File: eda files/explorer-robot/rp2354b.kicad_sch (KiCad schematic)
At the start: 31 parts, among them J1 Conn_01x05, SW1 SW_Push, U1 RP2354B, U2 AMS1117-3.3, Y1 ABM8-272-T3

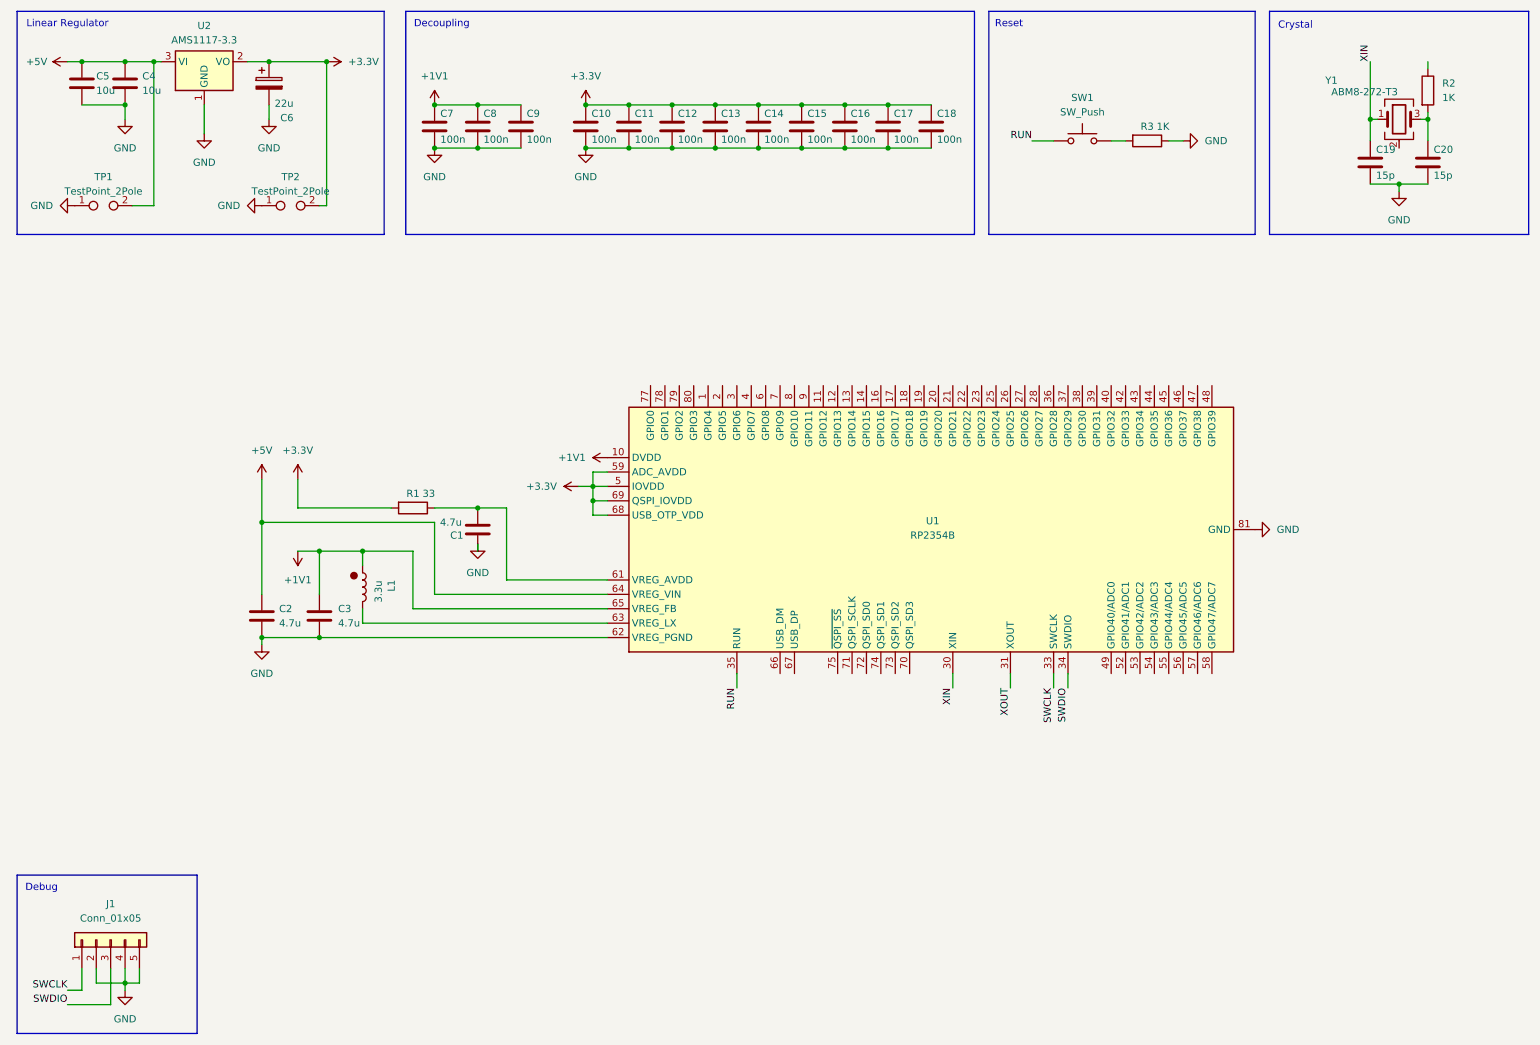
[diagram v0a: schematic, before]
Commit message: finish schematic for ICM-20948; requiring changes to pin assignment
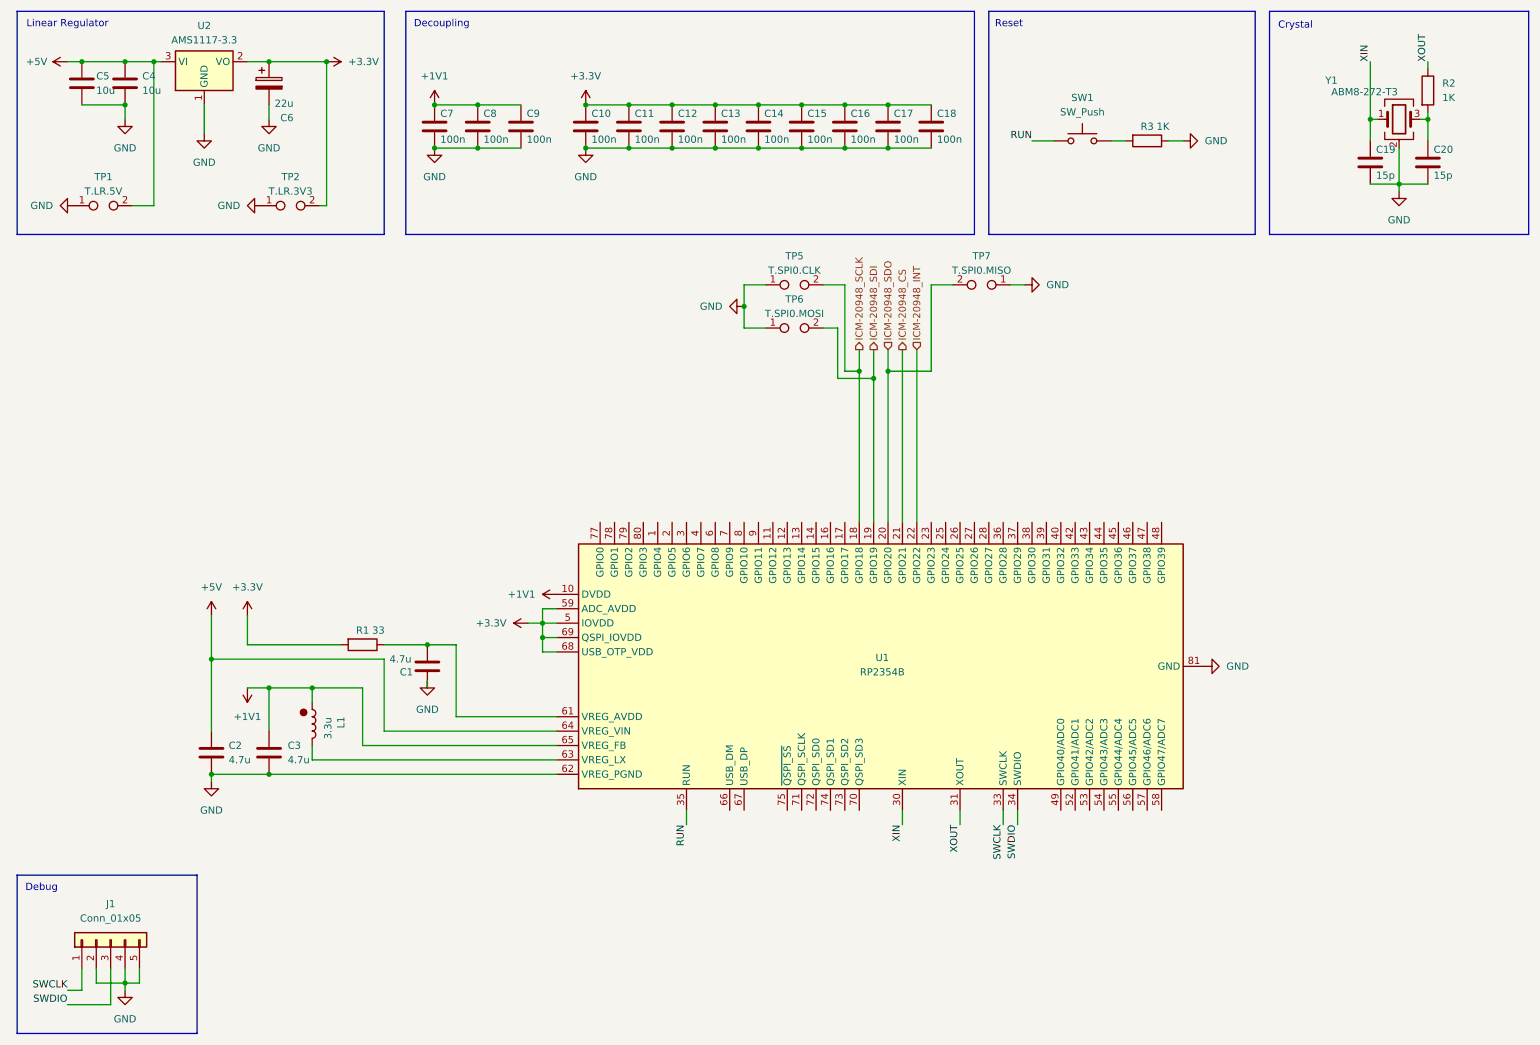
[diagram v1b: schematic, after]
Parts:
- added TP5: T.SPI0.CLK, tp:TestPoint_Bridge_Pitch3.81mm_Drill1.3mm, symbol Connector:TestPoint_2Pole
- added TP6: T.SPI0.MOSI, tp:TestPoint_Bridge_Pitch3.81mm_Drill1.3mm, symbol Connector:TestPoint_2Pole
- added TP7: T.SPI0.MISO, tp:TestPoint_Bridge_Pitch3.81mm_Drill1.3mm, symbol Connector:TestPoint_2Pole
- C1, C2, C3: LCSC https://jlcpcb.com/partdetail/24469-CL05A475MP5NRNC/C23733 -> C23733; MFR (none) -> Samsung Electro-Mechanics
- C10, C11, C12, C13, C14, C15, C16, C17, C18, C7, C8, C9: LCSC https://jlcpcb.com/partdetail/YAGEO-CC0603KRX7R9BB104/C14663 -> C14663; MFR (none) -> YAGEO; MPN C14663 -> CC0603KRX7R9BB104
- C19, C20: MFR (none) -> Samsung Electro-Mechanics
- C4, C5: LCSC https://jlcpcb.com/partdetail/20411-CL10A106KP8NNNC/C19702 -> C19702; MFR (none) -> Samsung Electro-Mechanics; MPN C19702 -> CL10A106KP8NNNC
- C6: LCSC https://jlcpcb.com/partdetail/-TAJA226K010RNJ/C11366 -> C11366; MFR (none) -> --; MPN C11366 -> TAJA226K010RNJ
- J1: LCSC https://jlcpcb.com/partdetail/Megastar-ZX_SH1_03PLT/C7430452 -> C7430452; MFR (none) -> Megastar; MPN C7430452 -> ZX-SH1.0-3PLT
- L1: LCSC https://jlcpcb.com/partdetail/AbraconLLC-AOTA_B201610S3R3_1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 -> C42411119; MFR (none) -> Abracon LLC; MPN C42411119 -> AOTA-B201610S3R3-101-T
- R1: LCSC https://jlcpcb.com/partdetail/25848-0402WGF330JTCE/C25105 -> 0402WGF330JTCE; MFR (none) -> UNI-ROYAL(Uniroyal Elec)
- R2: LCSC https://jlcpcb.com/partdetail/21904-0603WAF1001T5E/C21190 -> C21190; MFR (none) -> UNI-ROYAL(Uniroyal Elec); MPN C21190 -> 0603WAF1001T5E
- R3: LCSC https://jlcpcb.com/partdetail/12256-0402WGF1001TCE/C11702 -> C11702; MFR (none) -> UNI-ROYAL(Uniroyal Elec); MPN C11702 -> 0402WGF1001TCE
- SW1: LCSC https://jlcpcb.com/partdetail/XUNPU-TS_1088AR02016/C720477 -> C720477; MFR (none) -> XUNPU; MPN C720477 -> TS-1088-AR02016
- TP1: value TestPoint_2Pole -> T.LR.5V; footprint TestPoint:TestPoint_2Pads_Pitch5.08mm_Drill1.3mm -> tp:TestPoint_Bridge_Pitch3.81mm_Drill1.3mm
- TP2: value TestPoint_2Pole -> T.LR.3V3; footprint TestPoint:TestPoint_2Pads_Pitch5.08mm_Drill1.3mm -> tp:TestPoint_Bridge_Pitch3.81mm_Drill1.3mm
- U1: MFR (none) -> Raspberry Pi; MPN C39843328 -> RP2354B
- U2: LCSC https://jlcpcb.com/partdetail/Advanced_MonolithicSystems-AM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 -> C6186; MFR (none) -> Advanced Monolithic Systems; MPN C6186 -> AMS1117-3.3
- Y1: LCSC https://jlcpcb.com/partdetail/AbraconLLC-ABM8_272T3/C206257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 -> C20625731; MFR (none) -> Abracon LLC; MPN C20625731 -> ABM8-272-T3
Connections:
- net GND: now also Y1.2 (G), Y1.4 (G), TP5.1, TP6.1, TP7.1
- net XOUT: now also R2.1
- net ICM-20948_SCLK: now reaches U1.18 (GPIO18)
- net ICM-20948_SCLK: now also TP5.2
- net ICM-20948_SDI: now reaches U1.19 (GPIO19)
- net ICM-20948_SDI: now also TP6.2
- net ICM-20948_SDO: now reaches U1.20 (GPIO20)
- net ICM-20948_SDO: now also TP7.2
- net ICM-20948_CS: now reaches U1.21 (GPIO21)
- net ICM-20948_INT: now reaches U1.22 (GPIO22)
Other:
- title: (none) -> rp2354b and supporting components
- moved on the sheet: C1, C2, C3, L1, R1, U1

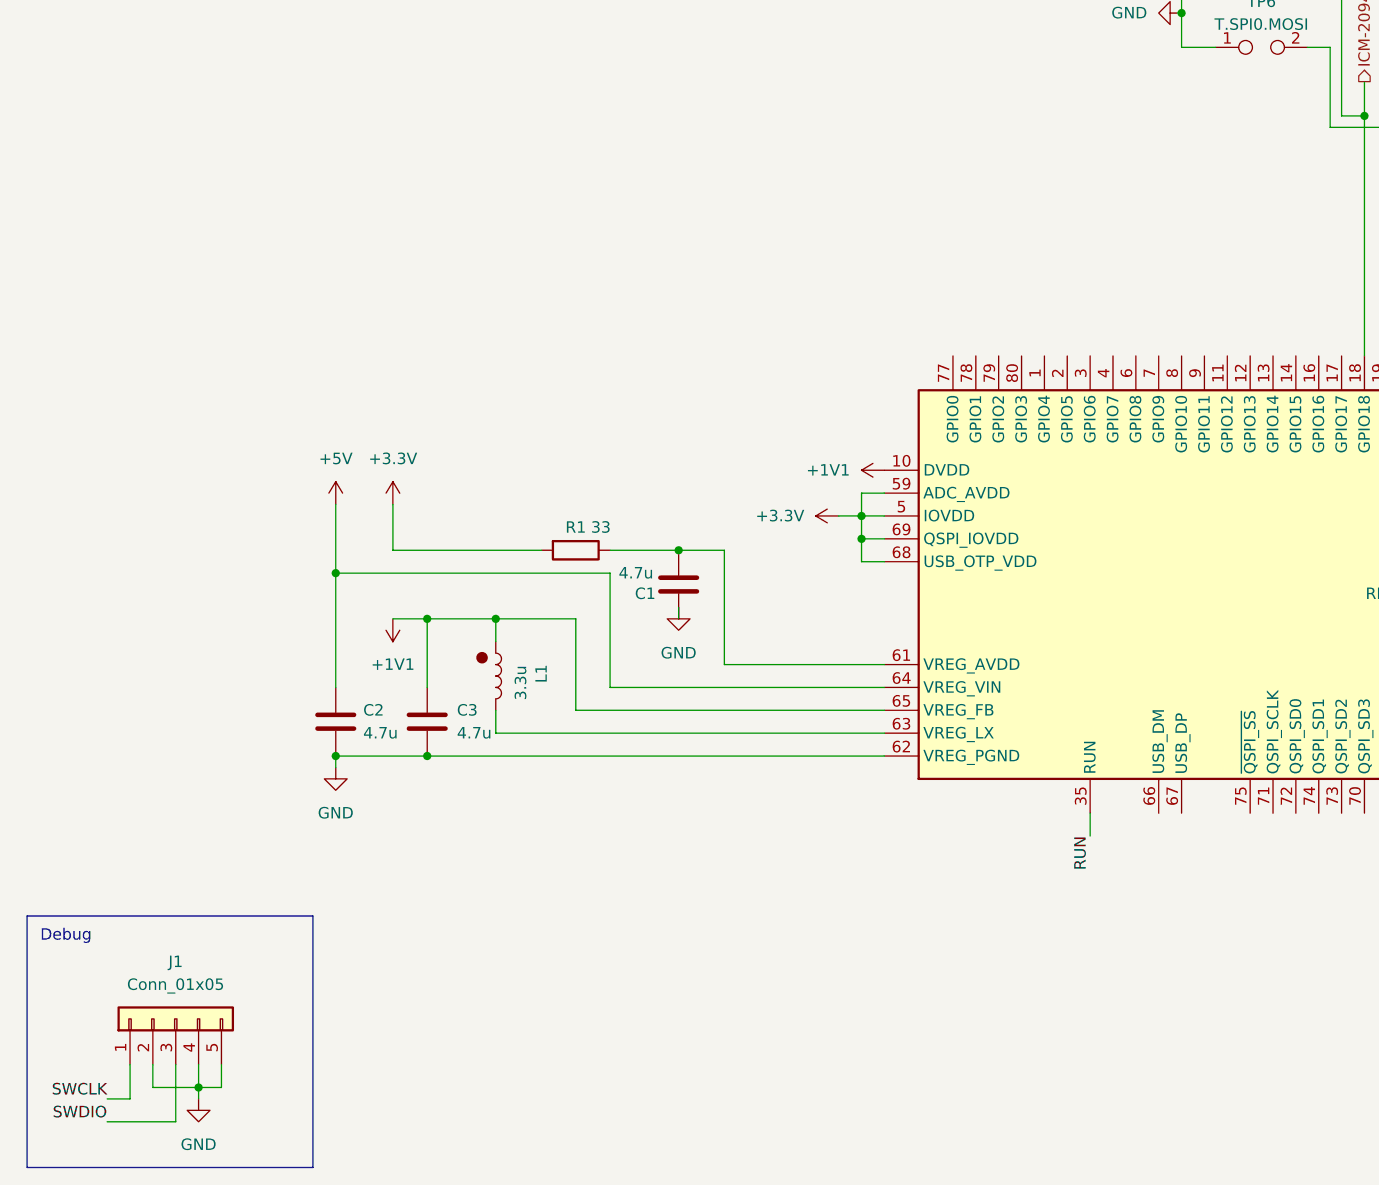
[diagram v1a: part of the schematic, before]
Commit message: Split power and motor driver into dedicated schematic sheets
Add ADRs 0018–0020 covering ground topology, battery rail and
connector protection decisions. Move battery, 5 V buck and test points
to a new power_and_batt sheet, and the TB6612FNG with motor connectors
to a new tb6612fng sheet.

Collapse the single ground net at the TB6612FNG, add the three-tier VM
decoupling stack and bidirectional TVS clamps on the motor pairs and VM.
Switch the 5 V rail to a TPS5430DDAR with a 220 µF/25 V polymer bulk
shared across the battery, VM and 5 V rails. Fix the ICM-20948 regulator
symbol to AMS1117-1.8.
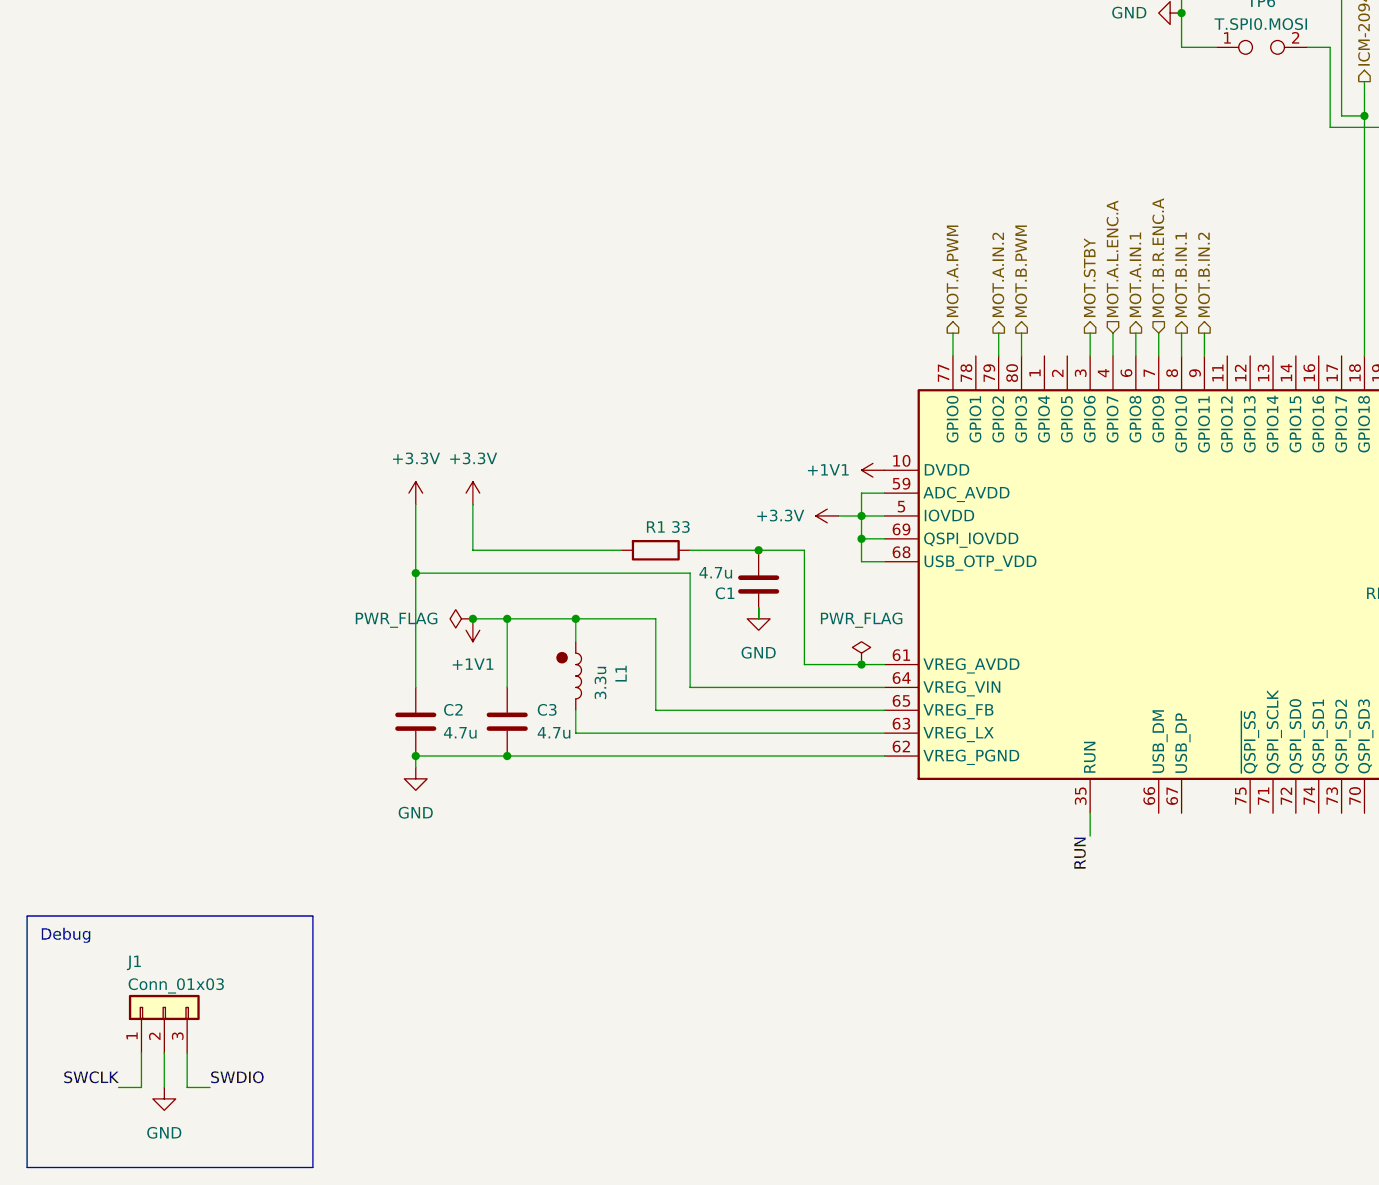
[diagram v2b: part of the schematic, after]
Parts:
- removed J1: Conn_01x05, Connector_JST:JST_SH_BM03B-SRSS-TB_1x03-1MP_P1.00mm_Vertical, symbol Connector_Generic:Conn_01x05
- added J1: Conn_01x03, Connector_JST:JST_SH_BM03B-SRSS-TB_1x03-1MP_P1.00mm_Vertical, symbol Connector_Generic:Conn_01x03
- C10, C11, C12, C13, C14, C15, C16, C17, C18, C4, C5, C7, C8, C9: footprint Capacitor_SMD:C_0201_0603Metric -> Capacitor_SMD:C_0603_1608Metric
- C19, C20: footprint Capacitor_SMD:C_0201_0603Metric -> Capacitor_SMD:C_0603_1608Metric; LCSC https://jlcpcb.com/partdetail/1996-CL10C150JB8NNNC/C1644 -> C1644; MPN C1644 -> CL10C150JB8NNNC
- R1: footprint Resistor_SMD:R_01005_0402Metric -> Resistor_SMD:R_0402_1005Metric; LCSC 0402WGF330JTCE -> C25105
- R3: footprint Resistor_SMD:R_01005_0402Metric -> Resistor_SMD:R_0402_1005Metric
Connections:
- net +3.3V: now also C2.1, U1.15 (IOVDD), U1.24 (IOVDD), U1.29 (IOVDD), U1.41 (IOVDD), U1.50 (IOVDD), U1.60 (IOVDD), U1.64 (VREG_VIN), U1.76 (IOVDD)
- net +5V: no longer C2.1, U1.64 (VREG_VIN)
- net GND: now also J1.2 (Pin_2)
- net SWCLK: now also J1.1 (Pin_1)
- net SWDIO: now also J1.3 (Pin_3)
- net MOT.STBY: now reaches U1.3 (GPIO6)
- net MOT.A.L.ENC.A: now reaches U1.4 (GPIO7)
- net MOT.A.IN.1: now reaches U1.6 (GPIO8)
- net MOT.B.R.ENC.A: now reaches U1.7 (GPIO9)
- net MOT.A.PWM: now reaches U1.77 (GPIO0)
- net MOT.A.IN.2: now reaches U1.79 (GPIO2)
- net MOT.B.IN.1: now reaches U1.8 (GPIO10)
- net MOT.B.PWM: now reaches U1.80 (GPIO3)
- net MOT.B.IN.2: now reaches U1.9 (GPIO11)
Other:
- moved on the sheet: C1, C2, C3, L1, R1

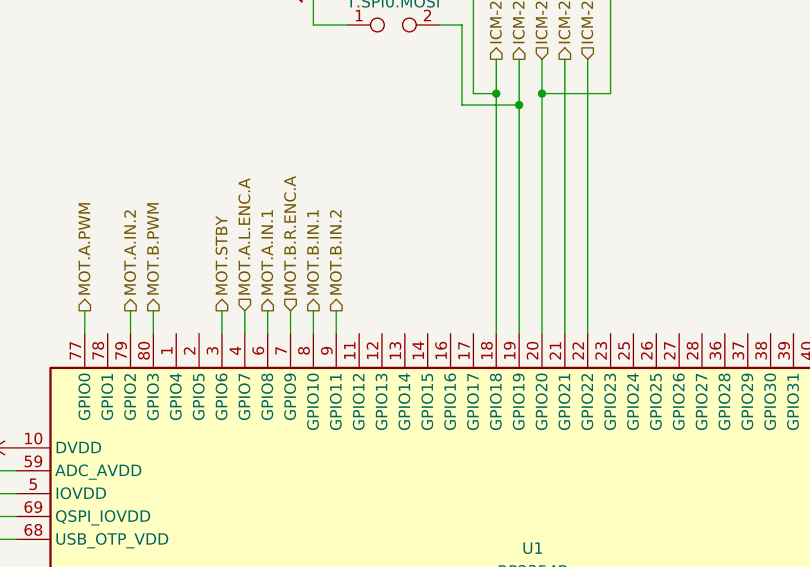
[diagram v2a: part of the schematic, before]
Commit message: Add ADR-0021 for expansion UART and camera on PIO
Add an RGB LED connector sheet to the schematic.
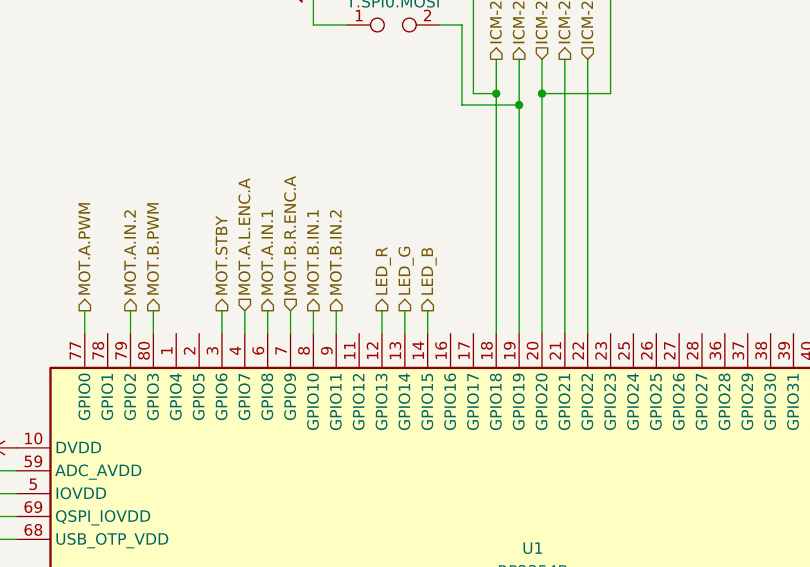
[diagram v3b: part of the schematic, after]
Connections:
- net LED_R: now reaches U1.12 (GPIO13)
- net LED_G: now reaches U1.13 (GPIO14)
- net LED_B: now reaches U1.14 (GPIO15)
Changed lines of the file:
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@@
+	(wire
+		(pts
+			(xy 151.13 102.87) (xy 151.13 105.41)
+		)
+		(stroke
+			(width 0)
+			(type default)
+		)
+	)
 	(wire
 		(pts
@@
 	(wire
 		(pts
+			(xy 153.67 102.87) (xy 153.67 105.41)
+		)
+		(stroke
+			(width 0)
+			(type default)
+		)
+	)
+	(wire
+		(pts
 			(xy 96.52 39.37) (xy 104.14 39.37)
 		)
@@
 		(pts
 			(xy 176.53 31.75) (xy 168.91 31.75)
+		)
+		(stroke
+			(width 0)
+			(type default)
+		)
+	)
+	(wire
+		(pts
+			(xy 156.21 102.87) (xy 156.21 105.41)
 		)
 		(stroke
@@
 			)
 			(justify left bottom)
+		)
+	)
+	(hierarchical_label "LED_G"
+		(shape output)
+		(at 153.67 102.87 90)
+		(effects
+			(font
+				(size 1.27 1.27)
+			)
+			(justify left)
 		)
 	)
@@
 		)
 	)
+	(hierarchical_label "LED_R"
+		(shape output)
+		(at 151.13 102.87 90)
+		(effects
+			(font
+				(size 1.27 1.27)
+			)
+			(justify left)
+		)
+	)
 	(hierarchical_label "ICM-20948_SDO"
 		(shape input)
@@
 		(effects
 			(font
+				(size 1.27 1.27)
+			)
+			(justify left)
+		)
+	)
+	(hierarchical_label "LED_B"
+		(shape output)
+		(at 156.21 102.87 90)
+		(effects
+			(font
